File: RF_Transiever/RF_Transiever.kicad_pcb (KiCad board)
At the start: 4 copper layers, 46.1 x 31.4 mm, 48 parts, among them J1 Conn_01x08_Pin, J2 Conn_01x08_Pin, J3 CON-SMA-EDGE-SRP, U1 SX1278, U2 RFSW6024, U3 NC7SZ04M5X

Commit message: v1.0.0
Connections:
- C1 pad 1: Net-(U1-VR_ANA) -> Net-(U1-VR_DIG)
- U1 pad 4: Net-(U1-VR_ANA) -> Net-(U1-VR_DIG)
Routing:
- net Net-(U1-VR_ANA): track 6.41 -> 1.26 mm, vias 2 -> 0
- net Net-(U1-VR_DIG): track 0.00 -> 2.28 mm
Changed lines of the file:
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@@
 	(net 46 "Net-(C22-Pad1)")
 	(net 47 "Net-(C23-Pad1)")
+	(net 48 "Net-(U1-VR_DIG)")
 	(footprint "MountingHole:MountingHole_2.2mm_M2_Pad"
 		(layer "F.Cu")
@@
 			(layers "F.Cu" "F.Mask" "F.Paste")
 			(roundrect_rratio 0.25)
-			(net 1 "Net-(U1-VR_ANA)")
+			(net 48 "Net-(U1-VR_DIG)")
 			(pintype "passive")
 		)
@@
 			(layers "F.Cu" "F.Mask" "F.Paste")
 			(roundrect_rratio 0.25)
-			(net 1 "Net-(U1-VR_ANA)")
+			(net 48 "Net-(U1-VR_DIG)")
 			(pinfunction "VR_DIG")
 			(pintype "power_in")
@@
 	)
 	(segment
-		(start 114.1 90.98)
-		(end 114 90.88)
-		(width 0.3)
-		(layer "F.Cu")
-		(net 1)
-	)
-	(segment
-		(start 115.1 92.05826)
-		(end 115.1 92.5125)
-		(width 0.3)
-		(layer "F.Cu")
-		(net 1)
-	)
-	(segment
-		(start 114 90.88)
-		(end 114 90.95826)
-		(width 0.3)
-		(layer "F.Cu")
-		(net 1)
-	)
-	(segment
 		(start 116.4 92.5125)
 		(end 116.4 91.25)
@@
 	)
 	(segment
-		(start 114.15 90.98)
-		(end 114.1 90.98)
-		(width 0.3)
-		(layer "F.Cu")
-		(net 1)
-	)
-	(segment
-		(start 114 90.95826)
-		(end 115.1 92.05826)
-		(width 0.3)
-		(layer "F.Cu")
-		(net 1)
-	)
-	(via
-		(at 116.4 91.25)
-		(size 0.7)
-		(drill 0.35)
-		(layers "F.Cu" "B.Cu")
-		(net 1)
-	)
-	(via
-		(at 114 90.88)
-		(size 0.7)
-		(drill 0.35)
-		(layers "F.Cu" "B.Cu")
-		(net 1)
-	)
-	(segment
-		(start 114.36 90.52)
-		(end 115.7 90.52)
-		(width 0.3)
-		(layer "B.Cu")
-		(net 1)
-	)
-	(segment
-		(start 114 90.88)
-		(end 114.36 90.52)
-		(width 0.3)
-		(layer "B.Cu")
-		(net 1)
-	)
-	(segment
-		(start 115.7 90.52)
-		(end 116.4 91.22)
-		(width 0.3)
-		(layer "B.Cu")
-		(net 1)
-	)
-	(segment
-		(start 116.4 91.22)
-		(end 116.4 91.25)
-		(width 0.3)
-		(layer "B.Cu")
-		(net 1)
-	)
-	(segment
 		(start 109.95 86.95)
 		(end 110.849998 87.849998)
@@
 		(net 47)
 	)
+	(segment
+		(start 114.1 90.98)
+		(end 114 90.88)
+		(width 0.3)
+		(layer "F.Cu")
+		(net 48)
+	)
+	(segment
+		(start 115.1 92.05826)
+		(end 115.1 92.5125)
+		(width 0.3)
+		(layer "F.Cu")
+		(net 48)
+	)
+	(segment
+		(start 114 90.88)
+		(end 114 90.95826)
+		(width 0.3)
+		(layer "F.Cu")
+		(net 48)
+	)
+	(segment
+		(start 114 90.95826)
+		(end 115.1 92.05826)
+		(width 0.3)
+		(layer "F.Cu")
+		(net 48)
+	)
+	(segment
+		(start 114.15 90.98)
+		(end 114.1 90.98)
+		(width 0.3)
+		(layer "F.Cu")
+		(net 48)
+	)
 	(zone

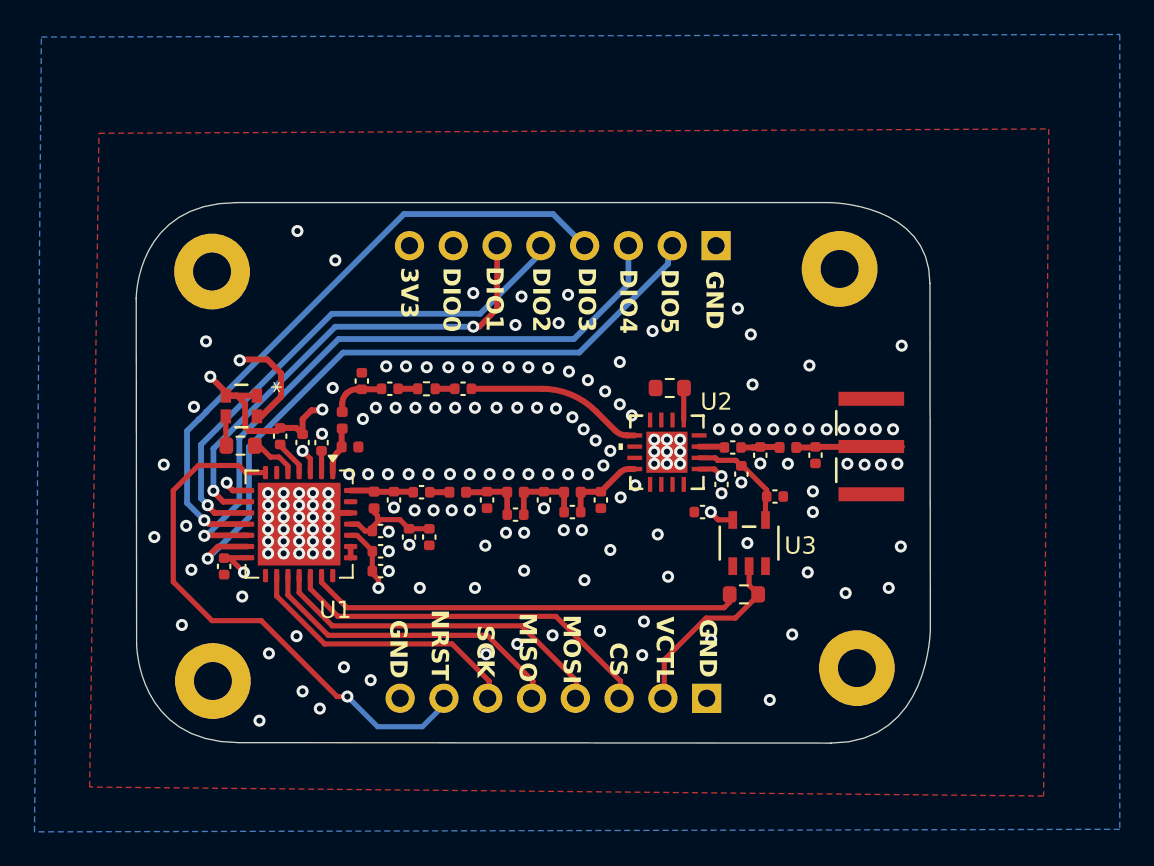
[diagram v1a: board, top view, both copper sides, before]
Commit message: Edge connector placement optimized, optimized power plane
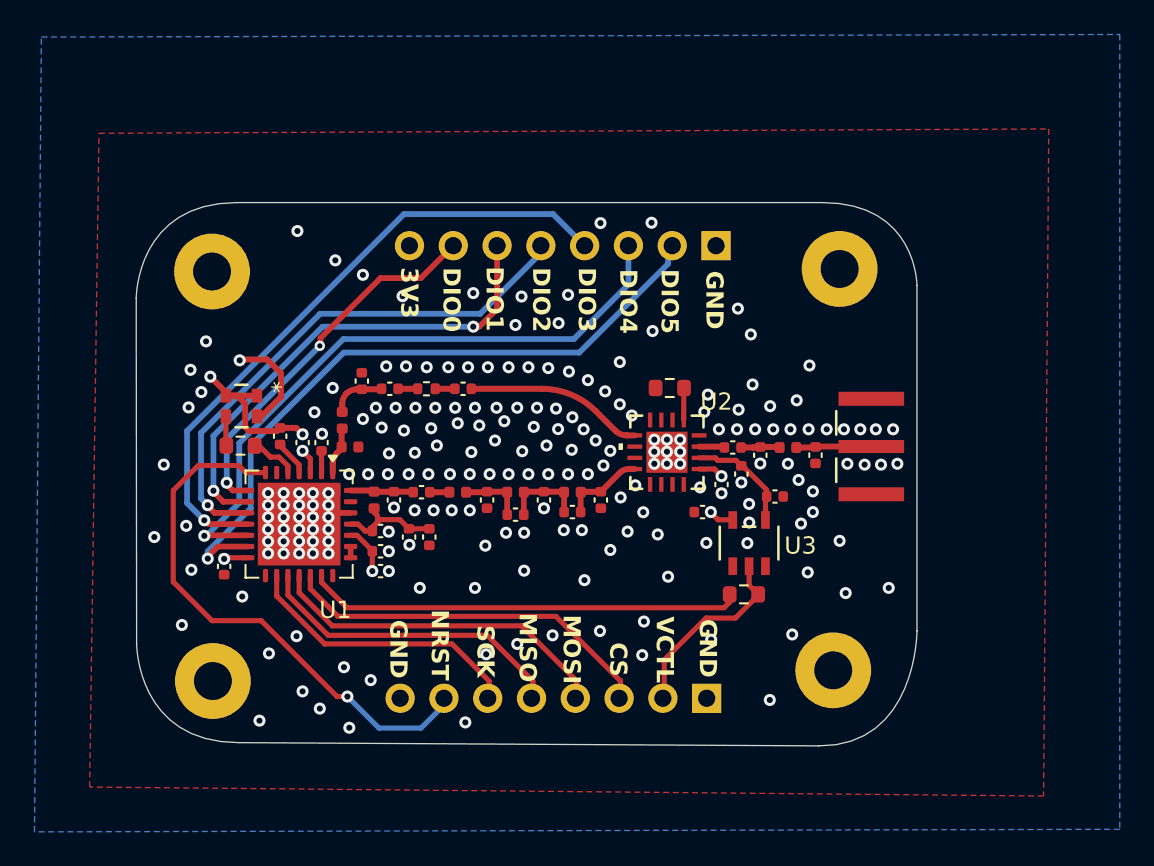
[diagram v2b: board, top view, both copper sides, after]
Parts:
- moved H4 1.38 mm to (146.1, 104.0)
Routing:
- net +3.3V: track 17.4 -> 14.8 mm
- net GND: track 14.7 -> 12.4 mm, vias 174 -> 211
- net DIO0: track 21.6 -> 22.0 mm, vias 1 -> 2
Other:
- board size 46.1 x 31.4 mm -> 45.3 x 31.5 mm
